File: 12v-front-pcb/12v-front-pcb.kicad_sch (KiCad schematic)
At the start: 31 parts, among them J1 172065-0208, J2 172065-0208, J3 172065-0208, J4 172065-0208

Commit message: Finalised 12v front PCB design (engine board) and sent for fabrication
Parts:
- removed BMS_FUSE1, DASHBOARD_FUSE1, HEATER_FAN_FUSE1, HORN_FUSE1, RADIO_FUSE1, VACUUM_PUMP_FUSE1: 178.6165.0001, Socket:17861650001, symbol Connector:178.6165.0001
- removed D1, D2: 10A10, Diode_THT:DIOAD1165W56L425D185, symbol Diode:10A10
- removed DASHBOARD_RELAY1, HORN_RELAY1, RADIO_RELAY1, VACUUM_RELAY1: DZ85AB-5-PCB, Connector:DZ85AB5PCB, symbol DZ85AB-5-PCB:DZ85AB-5-PCB
- removed H1, H5, H6: MountingHole, MountingHole:MountingHole_3mm, symbol Mechanical:MountingHole
- removed J1, J2, J3, J4: 172065-0208, Connector:1720650208, symbol Connector:172065-0208
- added D1, D2, D3: 1N5406, Diode_THT:D_DO-201AD_P15.24mm_Horizontal, symbol Diode:1N5406
- added ISA_SHUNT_FUSE1: 178.6165.0001, Socket:17861650001, symbol Connector:178.6165.0001
- added J1, J5, J7: 76825-0002, 768250002, symbol Connector:76825-0002
- added J2, J3, J4, J6: 76825-0004, 768250004, symbol Connector:76825-0004
- renumbered HVJB_FUSE1 to CONTACTORS_FUSE1
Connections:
- net CONTACTORS_12V: now also J4.2
- net IGNITION_SWITCH_B: now also J5.2
- net INVERTER_FWD: now also J2.3
- net INVERTER_REV: now also J2.1, J3.3
- net SHIFTER_FWD: now also J6.1
- net SHIFTER_REV: now also J6.4
- net 12V_BATT renamed 12V_BATT_IN
- net 12V_BATT_IN: now also COOLANT_PUMP_FUSE1.1, COOLANT_PUMP_FUSE1.2, COOLANT_PUMP_FUSE1.7, COOLANT_PUMP_FUSE1.8, INVERTER_FUSE1.1, INVERTER_FUSE1.2, INVERTER_FUSE1.7, INVERTER_FUSE1.8, ISA_SHUNT_FUSE1.1, ISA_SHUNT_FUSE1.2, ISA_SHUNT_FUSE1.7, ISA_SHUNT_FUSE1.8, J1.2, J5.1
- net BMS_FRONT_GND renamed CONTACTORS_GND
- net CONTACTORS_GND: now also J1.1, J2.4, J4.3, J4.4, J7.1
- net COOLANT_PUMP renamed COOLANT_12V
- net COOLANT_12V: now also J7.2
- net CRUISE_SWITCH_A renamed IGNITION_12V
- net IGNITION_12V: now also D1.2 (A), J6.3
- net DRIVE_INHIBIT: no longer names the net of FWD_DRIVE_INHIBIT_RELAY1.4, REV_DRIVE_INHIBIT_RELAY1.4
- net DRIVE_INHIBIT: now also D3.1 (K)
- removed net IGNITION_SWITCH_A: COOLANT_PUMP_FUSE1.1, COOLANT_PUMP_FUSE1.2, COOLANT_PUMP_FUSE1.7, COOLANT_PUMP_FUSE1.8, IGNITION_FUSE1.3, IGNITION_FUSE1.4, IGNITION_FUSE1.5, IGNITION_FUSE1.6, IGNITION_RELAY1.3, INVERTER_FUSE1.1, INVERTER_FUSE1.2, INVERTER_FUSE1.7, INVERTER_FUSE1.8
- net IGN_OR_CHARGE: no longer names the net of COOLANT_PUMP_RELAY1.4, INVERTER_RELAY1.4
- net IGN_OR_CHARGE: now also D1.1 (K), D2.1 (K)
- net INVERTER_12V renamed IGNITION_ENABLE_OUT
- net IGNITION_ENABLE_OUT: now also J2.2, J3.2
- new net: IGNITION_FUSE1.3, IGNITION_FUSE1.4, IGNITION_FUSE1.5, IGNITION_FUSE1.6, IGNITION_RELAY1.3
- new net CHARGER_ENABLE_IN: D2.2 (A), D3.2 (A), J3.1
- new net ISA_SHUNT_12V: ISA_SHUNT_FUSE1.3, ISA_SHUNT_FUSE1.4, ISA_SHUNT_FUSE1.5, ISA_SHUNT_FUSE1.6, J4.1
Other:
- note added: "12v + gnd to negative contactor gnd to precharge and main contactors"
- note added: "CABIN"
- note added: "HVJB"
- note added: "ISA"
- note added: "inverter"
- note added: "rear"
- note added: "shifter"
- note removed: "12v + gnd to shunt 12v + gnd to negative contactor gnd to precharge and main contactors"
- note removed: "BMS"
- note removed: "Battery heater"
- note removed: "DASHBOARD"
- note removed: "HEATER FAN"
- note removed: "HORN"
- note removed: "RADIO"
- note removed: "VACUUM"
- moved on the sheet: CONTACTORS_FUSE1, COOLANT_PUMP_FUSE1, COOLANT_PUMP_RELAY1, FWD_DRIVE_INHIBIT_RELAY1, IGNITION_FUSE1, IGNITION_RELAY1, INVERTER_FUSE1, INVERTER_RELAY1, REV_DRIVE_INHIBIT_RELAY1

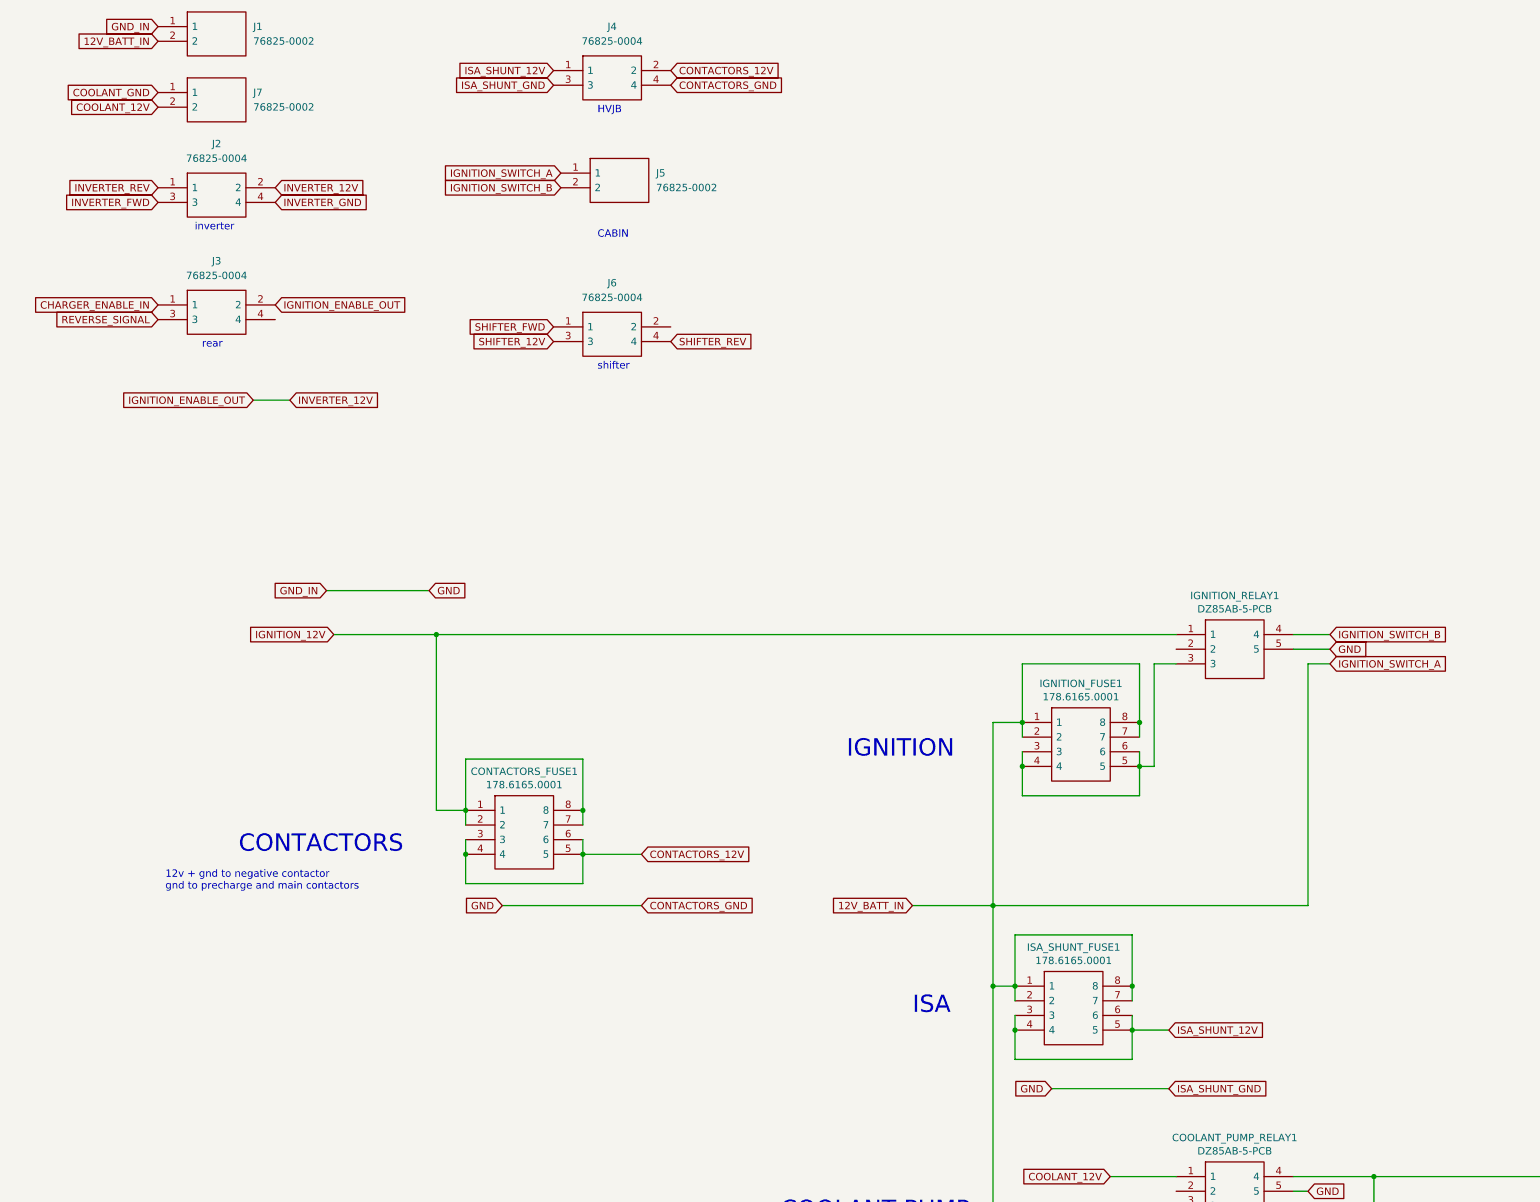
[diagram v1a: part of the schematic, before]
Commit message: Rework front PCB to make more room for relays
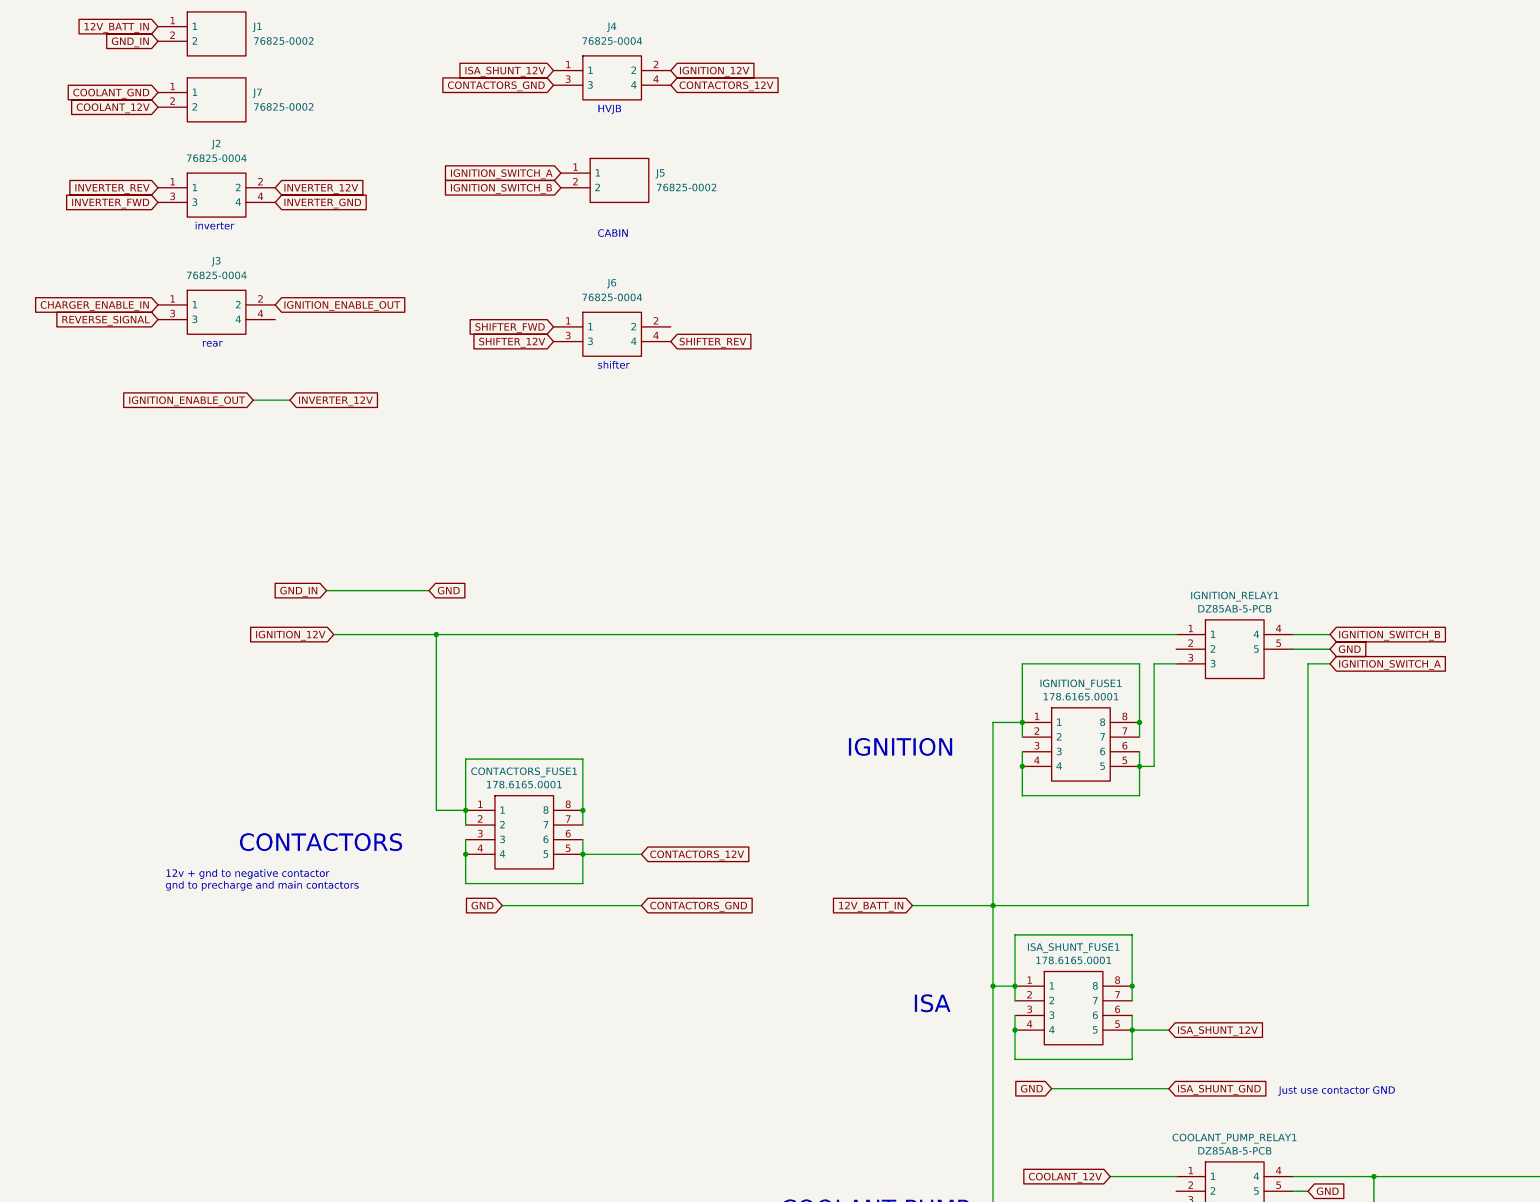
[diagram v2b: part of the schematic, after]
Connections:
- net 12V_BATT_IN: now also J1.1; no longer J1.2
- net CONTACTORS_12V: now also J4.4; no longer J4.2
- net CONTACTORS_GND: now also J1.2; no longer J1.1, J4.4
- net IGNITION_12V: now also J4.2
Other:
- note added: "Just use contactor GND"
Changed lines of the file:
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@@
   (junction (at 231.14 293.37) (diameter 0) (color 0 0 0 0)
   )
+  (junction (at 227.33 189.23) (diameter 0) (color 0 0 0 0)
+  )
+  (junction (at 251.46 245.11) (diameter 0) (color 0 0 0 0)
+  )
+  (junction (at 373.38 248.92) (diameter 0) (color 0 0 0 0)
+  )
+  (junction (at 251.46 237.49) (diameter 0) (color 0 0 0 0)
+  )
+  (junction (at 293.37 222.25) (diameter 0) (color 0 0 0 0)
+  )
+  (junction (at 389.89 229.87) (diameter 0) (color 0 0 0 0)
+  )
   (junction (at 252.73 143.51) (diameter 0) (color 0 0 0 0)
   )
-  (junction (at 227.33 189.23) (diameter 0) (color 0 0 0 0)
-  )
-  (junction (at 251.46 245.11) (diameter 0) (color 0 0 0 0)
-  )
-  (junction (at 373.38 248.92) (diameter 0) (color 0 0 0 0)
-  )
-  (junction (at 251.46 237.49) (diameter 0) (color 0 0 0 0)
-  )
-  (junction (at 293.37 222.25) (diameter 0) (color 0 0 0 0)
-  )
-  (junction (at 389.89 229.87) (diameter 0) (color 0 0 0 0)
-  )
   (junction (at 251.46 189.23) (diameter 0) (color 0 0 0 0)
   )
@@
     (stroke (width 0) (type default) (color 0 0 0 0))
   )
-  (wire (pts (xy 252.73 146.05) (xy 252.73 143.51))
-    (stroke (width 0) (type default) (color 0 0 0 0))
-  )
   (wire (pts (xy 279.4 128.27) (xy 285.75 128.27))
     (stroke (width 0) (type default) (color 0 0 0 0))
@@
     (stroke (width 0) (type default) (color 0 0 0 0))
   )
+  (wire (pts (xy 252.73 143.51) (xy 252.73 146.05))
+    (stroke (width 0) (type default) (color 0 0 0 0))
+  )
   (wire (pts (xy 279.4 224.79) (xy 281.94 224.79))
     (stroke (width 0) (type default) (color 0 0 0 0))
@@
     (stroke (width 0) (type default) (color 0 0 0 0))
   )
+  (wire (pts (xy 252.73 133.35) (xy 252.73 143.51))
+    (stroke (width 0) (type default) (color 0 0 0 0))
+  )
   (wire (pts (xy 231.14 250.19) (xy 251.46 250.19))
     (stroke (width 0) (type default) (color 0 0 0 0))
@@
   )
   (wire (pts (xy 231.14 189.23) (xy 231.14 180.34))
-    (stroke (width 0) (type default) (color 0 0 0 0))
-  )
-  (wire (pts (xy 252.73 133.35) (xy 252.73 143.51))
     (stroke (width 0) (type default) (color 0 0 0 0))
   )
@@
     (effects (font (size 2.9972 2.9972)) (justify left bottom))
   )
+  (text "Just use contactor GND" (at 276.86 208.28 0)
+    (effects (font (size 1.27 1.27)) (justify left bottom))
+  )
   (text "INVERTER" (at 200.66 290.83 0)
     (effects (font (size 2.9972 2.9972)) (justify left bottom))
@@
     )
   )
-  (global_label "12V_BATT_IN" (shape input) (at 82.55 25.4 180) (fields_autoplaced)
-    (effects (font (size 1.27 1.27)) (justify right))
-    (property "Intersheet References" "${INTERSHEET_REFS}" (id 0) (at 68.5539 25.3206 0)
+  (global_label "12V_BATT_IN" (shape input) (at 82.55 22.86 180) (fields_autoplaced)
+    (effects (font (size 1.27 1.27)) (justify right))
+    (property "Intersheet References" "${INTERSHEET_REFS}" (id 0) (at 68.5539 22.7806 0)
       (effects (font (size 1.27 1.27)) (justify right) hide)
     )
@@
     )
   )
-  (global_label "ISA_SHUNT_GND" (shape input) (at 151.13 33.02 180) (fields_autoplaced)
-    (effects (font (size 1.27 1.27)) (justify right))
-    (property "Intersheet References" "${INTERSHEET_REFS}" (id 0) (at 133.9287 33.0994 0)
-      (effects (font (size 1.27 1.27)) (justify right) hide)
-    )
-  )
   (global_label "CHARGER_ENABLE_IN" (shape input) (at 392.43 229.87 0) (fields_autoplaced)
     (effects (font (size 1.27 1.27)) (justify left))
@@
     )
   )
-  (global_label "CONTACTORS_12V" (shape input) (at 171.45 30.48 0) (fields_autoplaced)
-    (effects (font (size 1.27 1.27)) (justify left))
-    (property "Intersheet References" "${INTERSHEET_REFS}" (id 0) (at 190.2842 30.4006 0)
+  (global_label "CONTACTORS_12V" (shape input) (at 171.45 33.02 0) (fields_autoplaced)
+    (effects (font (size 1.27 1.27)) (justify left))
+    (property "Intersheet References" "${INTERSHEET_REFS}" (id 0) (at 190.2842 32.9406 0)
       (effects (font (size 1.27 1.27)) (justify left) hide)
     )
@@
     )
   )
-  (global_label "GND_IN" (shape input) (at 82.55 22.86 180) (fields_autoplaced)
-    (effects (font (size 1.27 1.27)) (justify right))
-    (property "Intersheet References" "${INTERSHEET_REFS}" (id 0) (at 73.4525 22.7806 0)
+  (global_label "GND_IN" (shape input) (at 82.55 25.4 180) (fields_autoplaced)
+    (effects (font (size 1.27 1.27)) (justify right))
+    (property "Intersheet References" "${INTERSHEET_REFS}" (id 0) (at 73.4525 25.3206 0)
       (effects (font (size 1.27 1.27)) (justify right) hide)
     )
@@
     )
   )
+  (global_label "IGNITION_12V" (shape input) (at 171.45 30.48 0) (fields_autoplaced)
+    (effects (font (size 1.27 1.27)) (justify left))
+    (property "Intersheet References" "${INTERSHEET_REFS}" (id 0) (at 240.03 62.23 0)
+      (effects (font (size 1.27 1.27)) hide)
+    )
+  )
   (global_label "COOLANT_GND" (shape input) (at 260.35 255.27 0) (fields_autoplaced)
     (effects (font (size 1.27 1.27)) (justify left))
@@
     )
   )
-  (global_label "CONTACTORS_GND" (shape input) (at 171.45 33.02 0) (fields_autoplaced)
-    (effects (font (size 1.27 1.27)) (justify left))
-    (property "Intersheet References" "${INTERSHEET_REFS}" (id 0) (at 190.6471 32.9406 0)
-      (effects (font (size 1.27 1.27)) (justify left) hide)
-    )
-  )
+  (global_label "CONTACTORS_GND" (shape input) (at 151.13 33.02 180) (fields_autoplaced)
+    (effects (font (size 1.27 1.27)) (justify right))
+    (property "Intersheet References" "${INTERSHEET_REFS}" (id 0) (at 131.9329 33.0994 0)
+      (effects (font (size 1.27 1.27)) (justify right) hide)
+    )
+  )

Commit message: Updates to the 12v front pcb
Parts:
- added BRAKE_FUSE1, CHARGING_CONTACTORS_FUSE1: 178.6165.0001, Socket:17861650001, symbol Connector:178.6165.0001
- added CHARGING_CONTACTORS1, FRONT_BATTERY_INHIBIT1, REAR_BATTERY_INHIBIT1: DZ85AB-5-PCB, Connector:DZ85AB5PCB, symbol DZ85AB-5-PCB:DZ85AB-5-PCB
- added J10: 76825-0002, 768250002, symbol Connector:76825-0002
- added J8, J9: 76825-0004, 768250004, symbol Connector:76825-0004
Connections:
- net 12V_BATT_IN: now also J1.2, J5.2, CHARGING_CONTACTORS_FUSE1.1, CHARGING_CONTACTORS_FUSE1.2, CHARGING_CONTACTORS_FUSE1.7, CHARGING_CONTACTORS_FUSE1.8; no longer J1.1, J5.1
- net CONTACTORS_GND: now also J1.1, CHARGING_CONTACTORS1.5, J8.4, J9.4; no longer J1.2, J4.3
- net IGNITION_12V: now also BRAKE_FUSE1.1, BRAKE_FUSE1.2, BRAKE_FUSE1.7, BRAKE_FUSE1.8
- net IGNITION_SWITCH_B: now also J5.1; no longer J5.2
- net at D3.1 (K), FWD_DRIVE_INHIBIT_RELAY1.4, REV_DRIVE_INHIBIT_RELAY1.4: now also CHARGING_CONTACTORS1.4, FRONT_BATTERY_INHIBIT1.4, REAR_BATTERY_INHIBIT1.4
- net at COOLANT_PUMP_RELAY1.4, D1.1 (K), D2.1 (K)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: now also FRONT_BATTERY_INHIBIT1.3, REAR_BATTERY_INHIBIT1.3
- new net: CHARGING_CONTACTORS1.3, CHARGING_CONTACTORS_FUSE1.3, CHARGING_CONTACTORS_FUSE1.4, CHARGING_CONTACTORS_FUSE1.5, CHARGING_CONTACTORS_FUSE1.6
- new net BRAKE_SWITCH_RETURN: J10.2
- new net BRAKE_SWITCH_SEND: BRAKE_FUSE1.3, BRAKE_FUSE1.4, BRAKE_FUSE1.5, BRAKE_FUSE1.6, J10.1
- new net FRONT_BATTERY_12V: CHARGING_CONTACTORS1.1, FRONT_BATTERY_INHIBIT1.2, J8.3, J9.3, REAR_BATTERY_INHIBIT1.2
- new net FRONT_BATTERY_INHIBIT: FRONT_BATTERY_INHIBIT1.5, J9.1
- new net HVJB_GND: J4.3
- new net REAR_BATTERY_INHIBIT: J8.1, REAR_BATTERY_INHIBIT1.5
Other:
- note added: "12V Battery"
- note added: "Brake switch"
- note added: "CHARGING CONTACTORS"
- note added: "Coolant pump"
- note added: "Front battery box"
- note added: "Rear battery box"
- note removed: "CABIN"
- moved on the sheet: CONTACTORS_FUSE1, COOLANT_PUMP_FUSE1, COOLANT_PUMP_RELAY1, D1, D2, D3, FWD_DRIVE_INHIBIT_RELAY1, H2, H3, H4, IGNITION_FUSE1, IGNITION_RELAY1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
